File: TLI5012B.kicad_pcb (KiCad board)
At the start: 2 copper layers, 22.9 x 20.3 mm, 2 parts, among them J1 Conn_01x08_Female, U1 TLI5012B

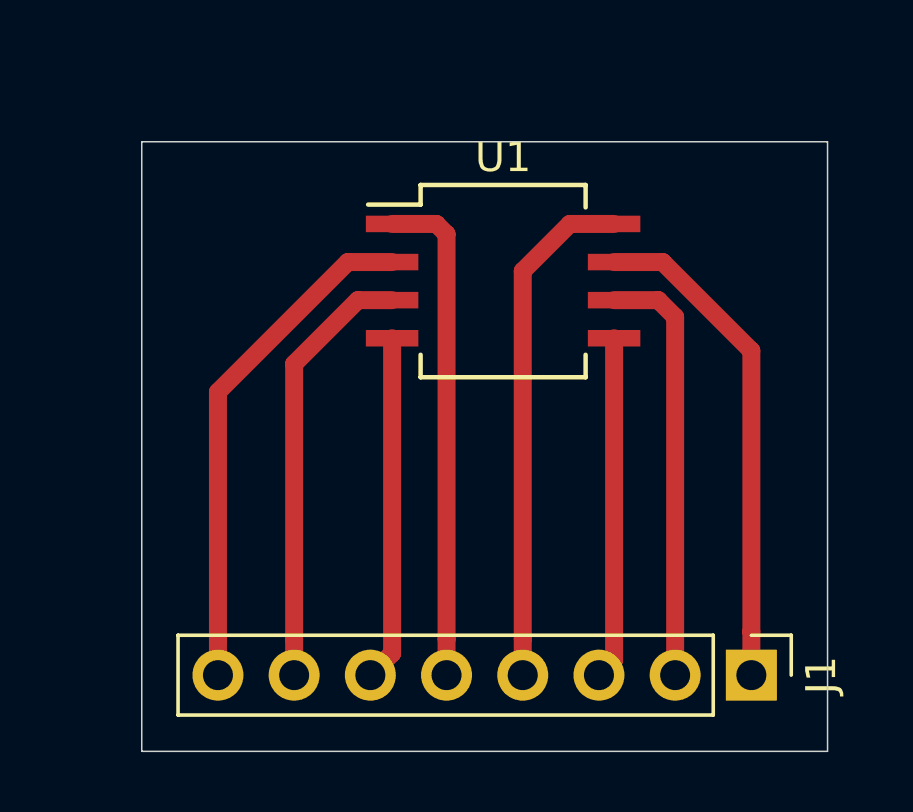
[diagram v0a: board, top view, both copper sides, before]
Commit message: smaller footprint fits better
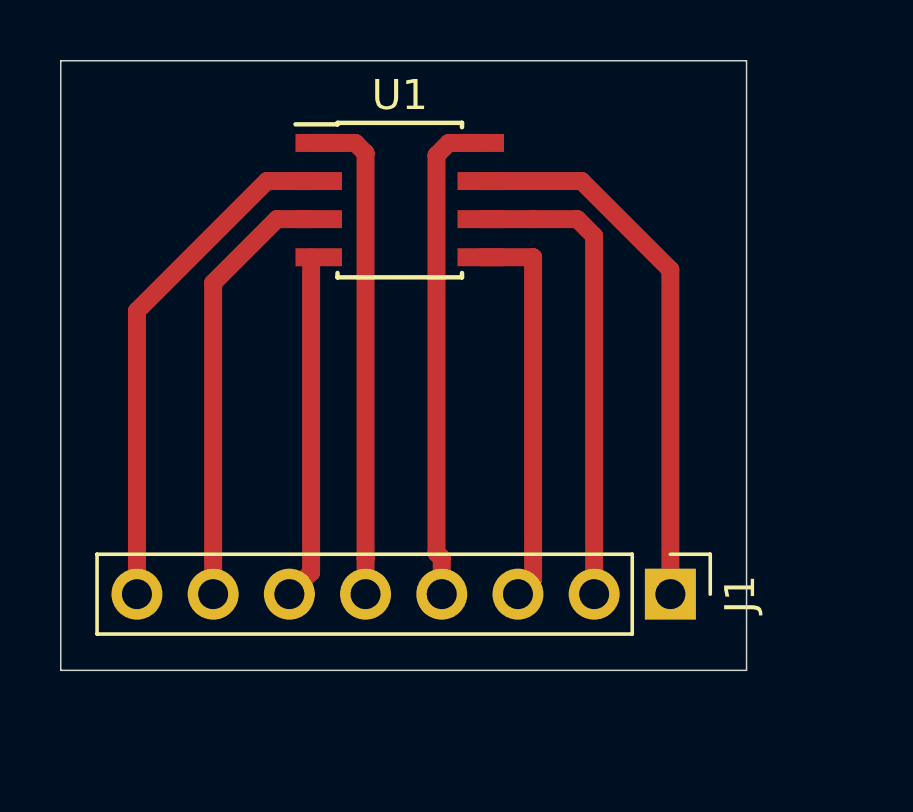
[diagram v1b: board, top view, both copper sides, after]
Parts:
- U1: footprint Package_SO:SO-8_5.3x6.2mm_P1.27mm -> Package_SO:SOIC-8_3.9x4.9mm_P1.27mm
- moved U1 4.38 mm to (21.3, 14.6)
- moved J1 3.82 mm to (30.3, 27.8)
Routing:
- net /VDD: track 14.2 -> 16.0 mm
- net /GND: track 16.6 -> 18.4 mm
- net /IFA: track 11.4 -> 13.2 mm
- net /IFB: track 17.2 -> 16.3 mm

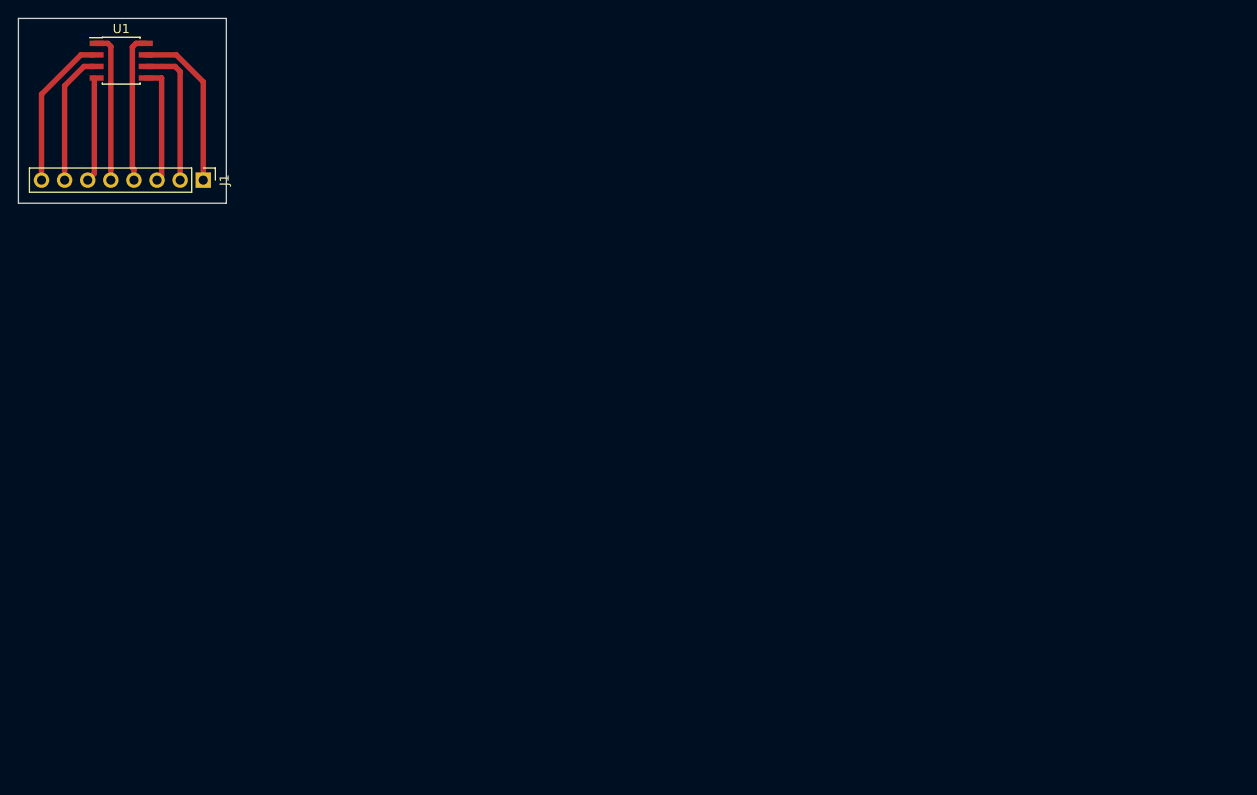
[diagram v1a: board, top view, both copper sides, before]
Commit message: with jst connector
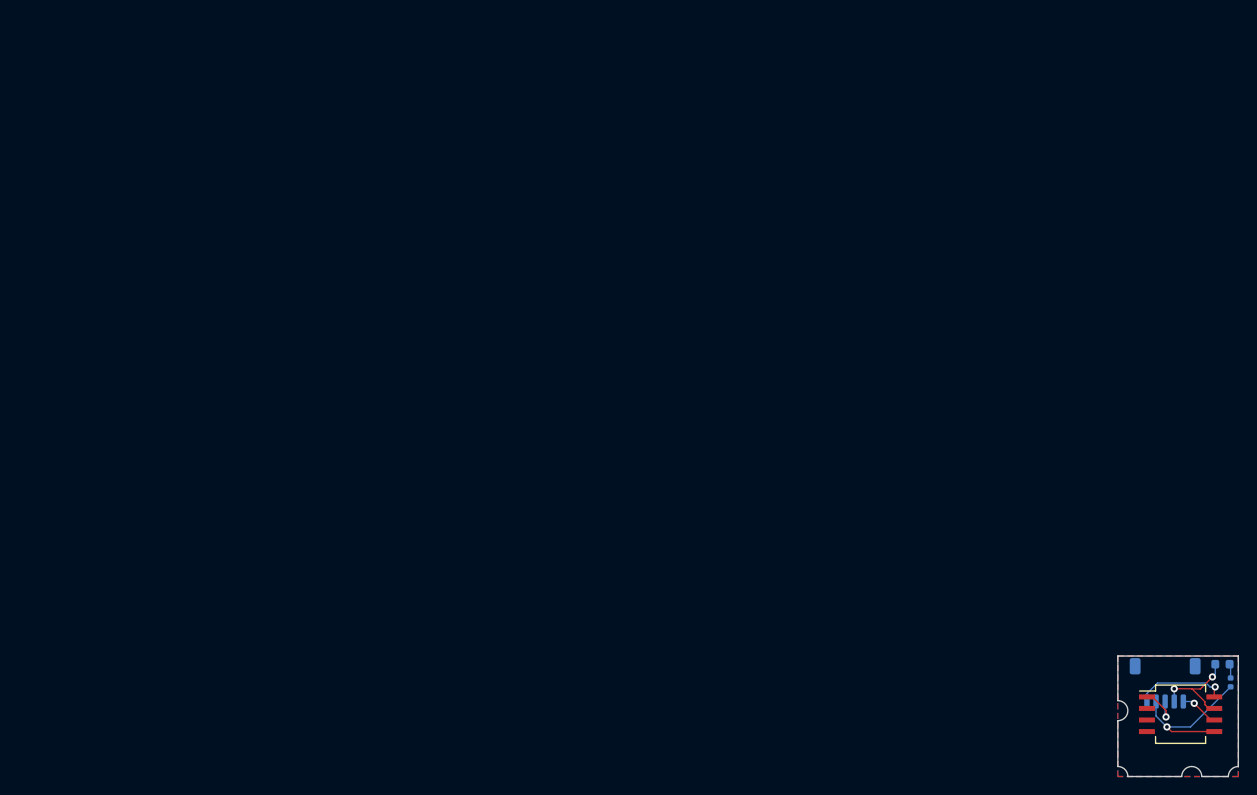
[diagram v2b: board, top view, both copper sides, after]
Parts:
- added D1: LED, LED_SMD:LED_0603_1608Metric, B.Cu at (142.4, 81.0)
- added R1: 1k, LED_SMD:LED_0402_1005Metric, B.Cu at (143.3, 83.0)
- J1: value Conn_01x08_Female -> Conn_01x05_Female; footprint Connector_PinHeader_2.54mm:PinHeader_1x08_P2.54mm_Vertical -> Connector_JST:JST_SH_SM05B-SRSS-TB_1x05-1MP_P1.00mm_Horizontal; moved to B.Cu
- U1: footprint Package_SO:SOIC-8_3.9x4.9mm_P1.27mm -> Package_SO:SO-8_5.3x6.2mm_P1.27mm
- moved U1 136.9 mm to (137.8, 86.5)
- moved J1 119.3 mm to (136.1, 83.1), turned to 0 degrees
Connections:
- J1 pad 1: /GND -> /IFB
- J1 pad 2: /VDD -> /IFA
- J1 pad 3: /IFA -> /IFC
- J1 pad 4: /IFB -> /GND
- J1 pad 5: /IFC -> /VDD
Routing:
- net /SCK: track 17.0 -> 0.00 mm
- net /CSQ: track 14.5 -> 0.00 mm
- net /VDD: track 16.0 -> 4.24 mm, vias 0 -> 1
- net /DATA: track 11.5 -> 0.00 mm
- net /IFC: track 16.7 -> 5.17 mm, vias 0 -> 1
- net /GND: track 18.4 -> 11.2 mm, vias 0 -> 2
- net /IFB: track 16.3 -> 10.2 mm, vias 0 -> 1
- net /IFA: track 13.2 -> 17.5 mm, vias 0 -> 1
- net Net-(D1-Pad2): track 0.00 -> 1.56 mm
- added copper zone on F.Cu, net +5V
- added copper zone on B.Cu, net GND
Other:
- board size 22.9 x 20.3 mm -> 13.2 x 13.2 mm
- net class Default: clearance 0.4 -> 0.1524; trace_width 0.6 -> 0.1524
- net class PWR added: clearance 0.1524, trace_width 0.254, via_dia 0.8, via_drill 0.4
- rule pad_to_mask_clearance: 0.051 -> 0.2
- rule trace_clearance: 0.4 -> 0.1524
- rule trace_min: 0.2 -> 0.1524

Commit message: pcbway order submitted
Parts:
- added G***: LOGO, custom_lib:R1_eyes_mask_5.5mm, B.Cu at (141.1, 89.8)
- added G***: LOGO, custom_lib:R1_face_mask_5.5mm, B.Cu at (141.1, 89.8)
- added G***: LOGO, custom_lib:R1_ear_silk_5.5mm, B.Cu at (141.1, 89.8)

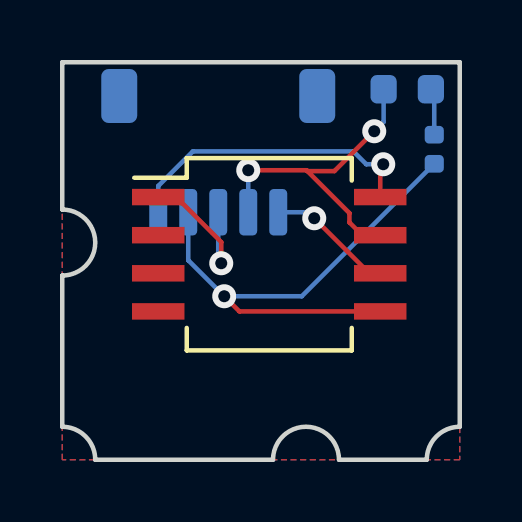
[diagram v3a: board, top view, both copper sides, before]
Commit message: with mounting holes
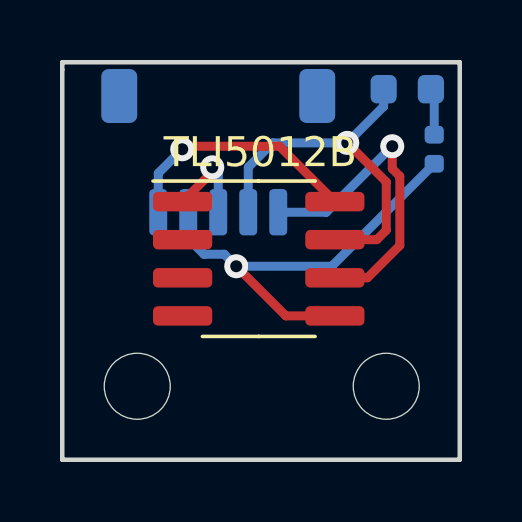
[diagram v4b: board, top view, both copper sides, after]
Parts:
- added REF**: MountingHole_2.2mm_M2, MountingHole:MountingHole_2.2mm_M2, F.Cu at (133.4, 90.9)
- added REF**: MountingHole_2.2mm_M2, MountingHole:MountingHole_2.2mm_M2, F.Cu at (141.7, 90.9)
- U1: footprint Package_SO:SO-8_5.3x6.2mm_P1.27mm -> Package_SO:SOP-8_3.76x4.96mm_P1.27mm
- moved G*** 3.54 mm to (137.6, 90.3), turned to 180 degrees (x3)
- moved U1 0.38 mm to (137.4, 86.7)
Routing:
- net /VDD: track 4.24 -> 10.8 mm
- net /IFA: track 17.5 -> 14.8 mm
- net /IFC: track 5.17 -> 3.13 mm
- net /IFB: track 10.2 -> 8.32 mm
- net /GND: track 11.2 -> 12.7 mm, vias 2 -> 1
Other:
- outline, holes or cut-outs redrawn
- net class Default: trace_width 0.1524 -> 0.3
- board text added: "TLI5012B"
